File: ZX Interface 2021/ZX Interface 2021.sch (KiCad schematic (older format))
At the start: 53 parts, among them J1 PORT 1, J2 PORT 2, J4 Extended Cartridge Port, J5 JOYSTICK_EN, M1 Mounting, M2 Mounting, M3 Mounting, M4 Mounting, M5 Mounting, M6 Mounting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

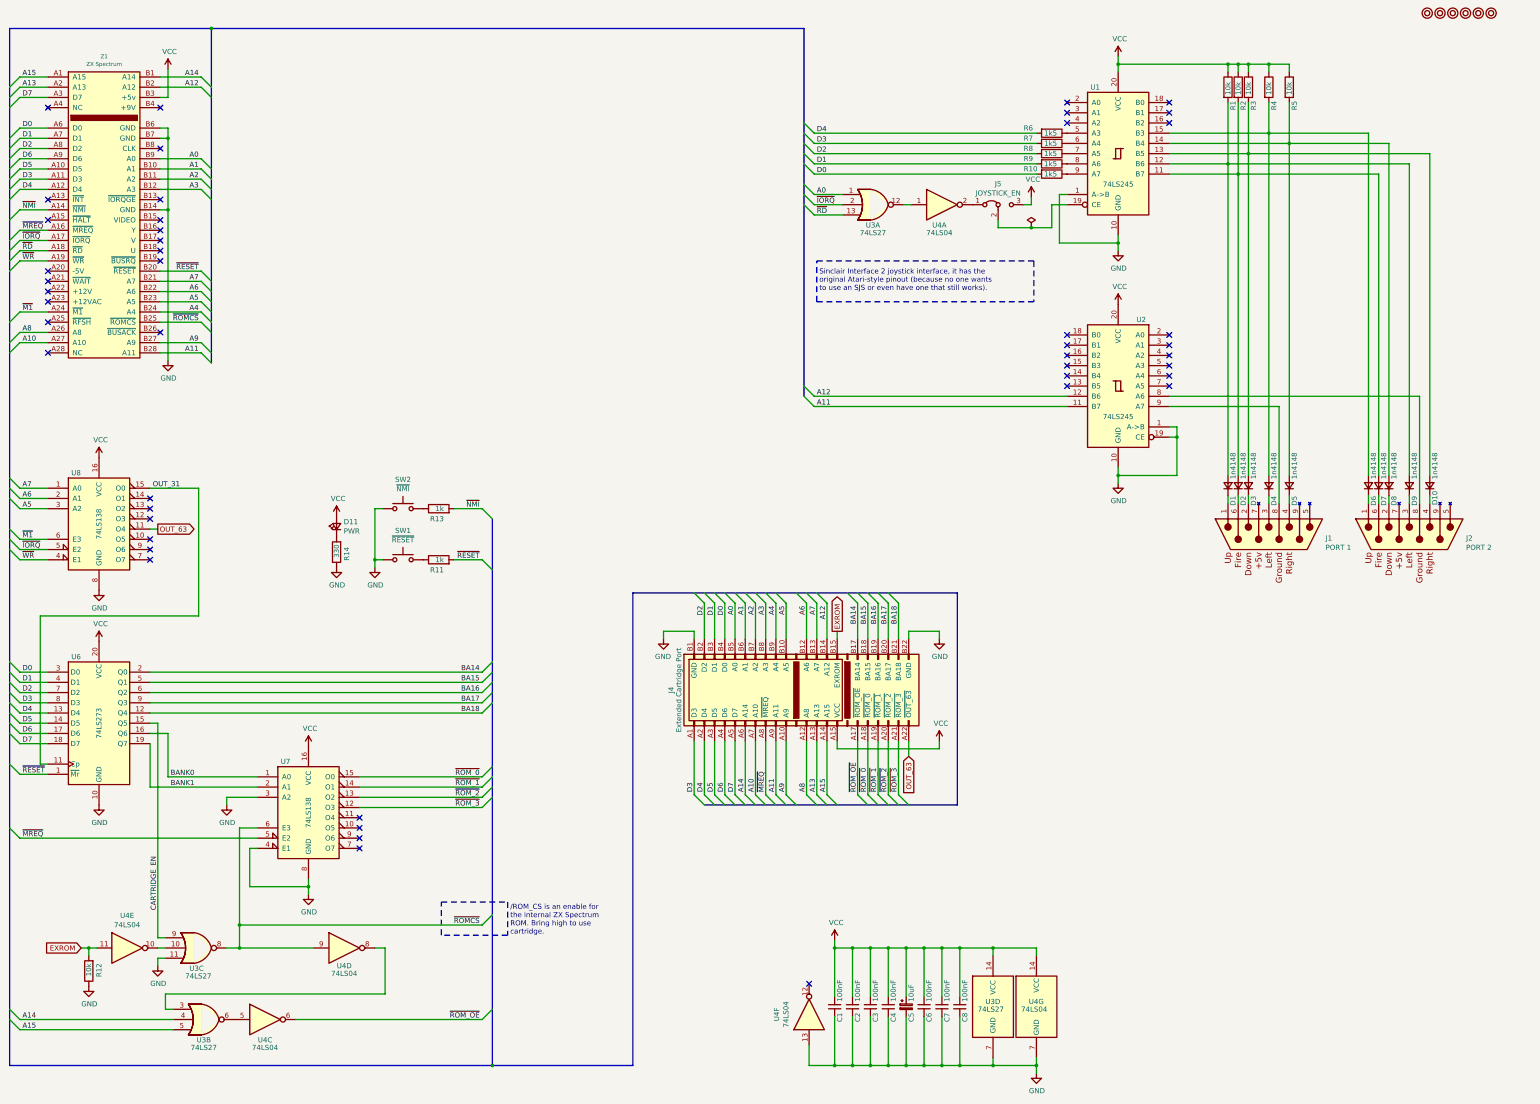
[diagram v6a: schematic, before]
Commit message: Made 74ls245 open collector instead of using resistors
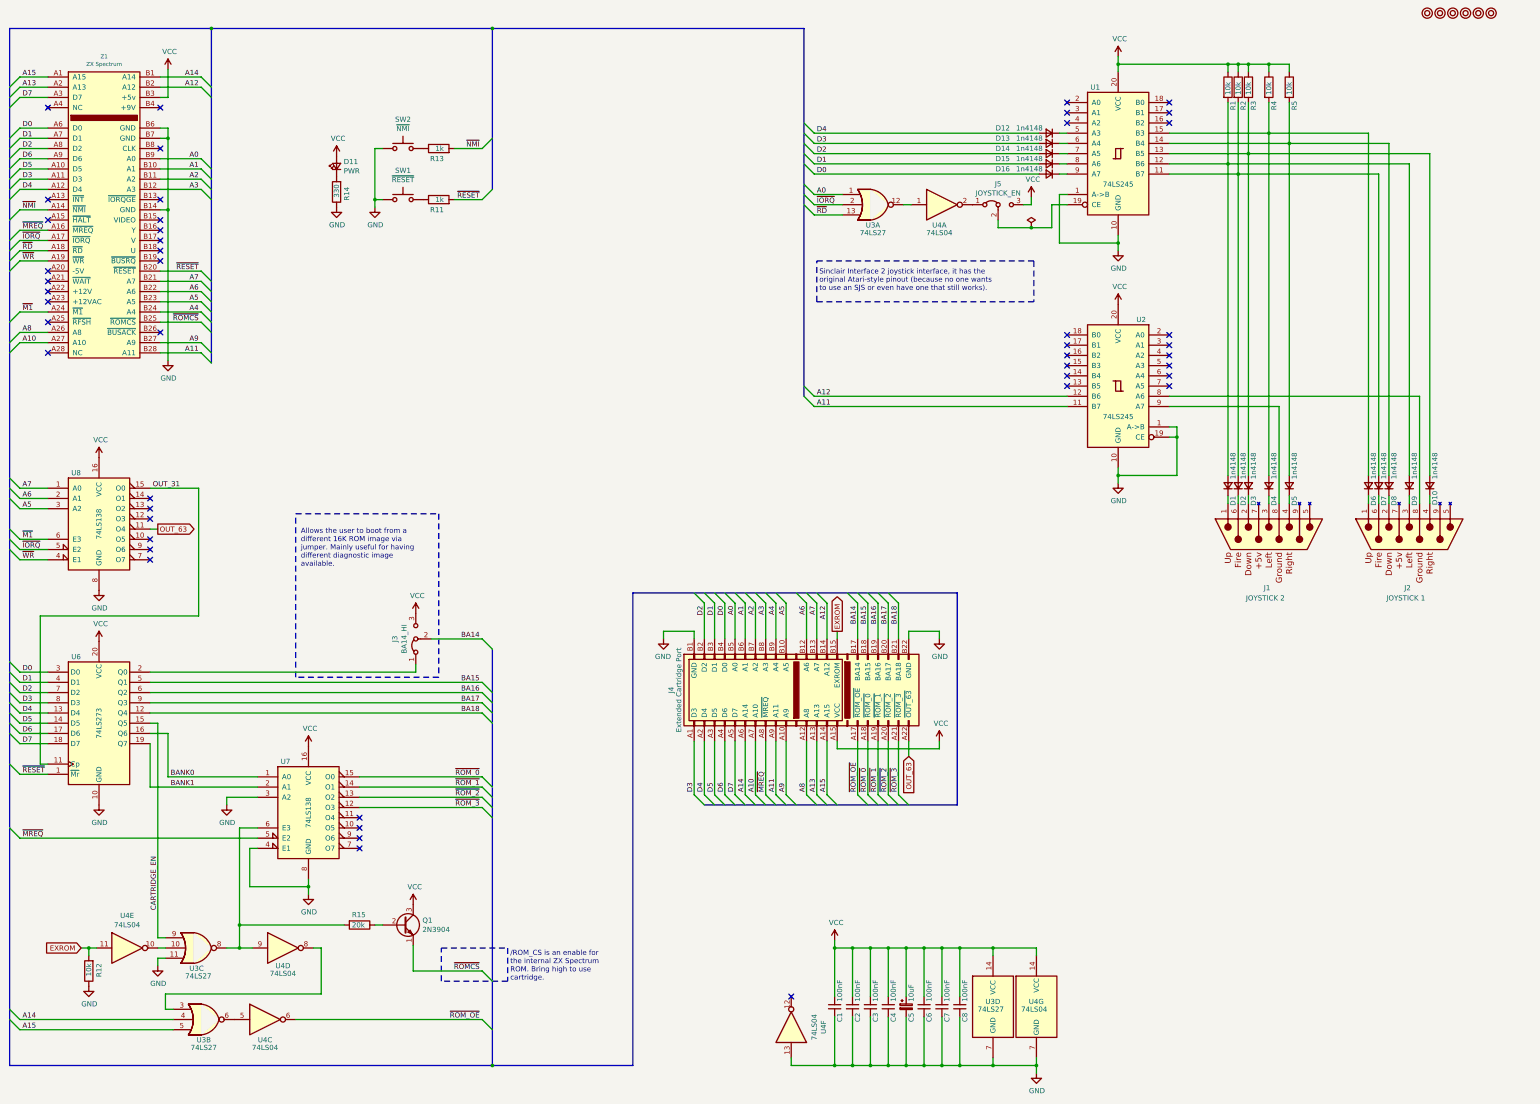
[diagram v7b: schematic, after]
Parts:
- removed R10, R6, R7, R8, R9: 1k5, Resistor_THT:R_Axial_DIN0207_L6.3mm_D2.5mm_P10.16mm_Horizontal, symbol Device:R
- added D12, D13, D14, D15, D16: 1n4148, 1n4148:D_DO-35_SOD27_P7.62mm_Horizontal, symbol Device:D_Small
- added J3: BA14_HI, Connector_PinHeader_2.54mm:PinHeader_1x03_P2.54mm_Horizontal, symbol solder_select:Jumper_3_Bridged12
- added Q1: 2N3904, Package_TO_SOT_THT:TO-92_Inline_Wide, symbol Transistor_BJT:2N3904
- added R15: 20k, Resistor_THT:R_Axial_DIN0207_L6.3mm_D2.5mm_P10.16mm_Horizontal, symbol Device:R
- J1: value PORT 1 -> JOYSTICK 2
- J2: value PORT 2 -> JOYSTICK 1
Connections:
- net BA14: now also J3.2 (C); no longer U6.2 (Q0)
- net D0: now also D16.2 (A)
- net D1: now also D15.2 (A)
- net D2: now also D14.2 (A)
- net D3: now also D13.2 (A)
- net D4: now also D12.2 (A)
- net VCC: now also J3.3 (B), Q1.3 (C)
- net ~ROMCS: now also Q1.1 (E); no longer U3.8, U4.9, U7.6 (E3)
- net at U1.5 (A3): now also D12.1 (K)
- net at U1.6 (A4): now also D13.1 (K)
- net at U1.7 (A5): now also D14.1 (K)
- net at U1.8 (A6): now also D15.1 (K)
- net at U1.9 (A7): now also D16.1 (K)
- new net: R15.2, U3.8, U4.9, U7.6 (E3)
- new net: Q1.2 (B), R15.1
- new net: J3.1 (A), U6.2 (Q0)
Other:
- note added: "Allows the user to boot from a\ndifferent 16K ROM image via\njumper. Mainly useful for having\ndifferent diagnostic image\navailable."
- moved on the sheet: D11, R11, R13, R14, SW1, SW2, U4D, U4F

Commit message: Cleanup
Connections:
- net at D7.2 (A), R2.2, U1.11 (B7): now also D4.2 (A); no longer D2.2 (A)
- net at D1.2 (A), R1.2: now also D10.2 (A), U1.14 (B4); no longer D9.2 (A), U1.12 (B6)
- net at D3.2 (A), R3.2, U1.13 (B5): now also D8.2 (A); no longer D10.2 (A)
- net at D5.2 (A), R5.2: now also D6.2 (A), U1.12 (B6); no longer D8.2 (A), U1.14 (B4)
- net at R4.2, U1.15 (B3): now also D2.2 (A), D9.2 (A); no longer D4.2 (A), D6.2 (A)
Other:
- note added: "0"
- note added: "1"
- note added: "2"
- note added: "3"
- note added: "4"
- note added: "5"
- note added: "6"
- note added: "7"
- note added: "8"
- note added: "9"
- note added: "b0"
- note added: "b1"
- note added: "b2"
- note added: "b3"
- note added: "b4"
- moved on the sheet: R2, R4
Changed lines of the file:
@@
 U 1 1 603A5F65
 P 13800 5650
-F 0 "J1" V 14325 5600 50  0000 L CNN
-F 1 "JOYSTICK 2" V 14425 5425 50  0000 L CNN
+F 0 "J1" V 14425 5600 50  0000 L CNN
+F 1 "JOYSTICK 2" V 14500 5425 50  0000 L CNN
 F 2 "RND_DSUB:DSUB-9_Male_Vertical_Pitch2.77x2.84mm" H 13800 5650 50  0001 C CNN
 F 3 "" H 13800 5650 50  0001 C CNN
@@
 U 1 1 603A8E5C
 P 15175 5650
-F 0 "J2" V 15700 5600 50  0000 L CNN
-F 1 "JOYSTICK 1" V 15800 5425 50  0000 L CNN
+F 0 "J2" V 15800 5600 50  0000 L CNN
+F 1 "JOYSTICK 1" V 15875 5425 50  0000 L CNN
 F 2 "RND_DSUB:DSUB-9_Male_Vertical_Pitch2.77x2.84mm" H 15175 5650 50  0001 C CNN
 F 3 "" H 15175 5650 50  0001 C CNN
@@
 L Device:R R2
 U 1 1 60412DFF
-P 13500 1275
-F 0 "R2" V 13550 1050 50  0000 L CNN
-F 1 "10k" V 13500 1200 50  0000 L CNN
-F 2 "Resistor_THT:R_Axial_DIN0207_L6.3mm_D2.5mm_P10.16mm_Horizontal" V 13430 1275 50  0001 C CNN
-F 3 "~" H 13500 1275 50  0001 C CNN
-	1    13500 1275
+P 13800 1275
+F 0 "R2" V 13850 1050 50  0000 L CNN
+F 1 "10k" V 13800 1200 50  0000 L CNN
+F 2 "Resistor_THT:R_Axial_DIN0207_L6.3mm_D2.5mm_P10.16mm_Horizontal" V 13730 1275 50  0001 C CNN
+F 3 "~" H 13800 1275 50  0001 C CNN
+	1    13800 1275
 	1    0    0    -1
 $EndComp
@@
 L Device:R R4
 U 1 1 60420784
-P 13800 1275
-F 0 "R4" V 13850 1050 50  0000 L CNN
-F 1 "10k" V 13800 1200 50  0000 L CNN
-F 2 "Resistor_THT:R_Axial_DIN0207_L6.3mm_D2.5mm_P10.16mm_Horizontal" V 13730 1275 50  0001 C CNN
-F 3 "~" H 13800 1275 50  0001 C CNN
-	1    13800 1275
+P 13500 1275
+F 0 "R4" V 13550 1050 50  0000 L CNN
+F 1 "10k" V 13500 1200 50  0000 L CNN
+F 2 "Resistor_THT:R_Axial_DIN0207_L6.3mm_D2.5mm_P10.16mm_Horizontal" V 13430 1275 50  0001 C CNN
+F 3 "~" H 13500 1275 50  0001 C CNN
+	1    13500 1275
 	1    0    0    -1
 $EndComp
@@
 	14000 5275 14000 5350
 Wire Wire Line
-	13800 5075 13800 1725
-Wire Wire Line
 	13600 5275 13600 5350
 Wire Wire Line
 	13500 5275 13500 5350
-Wire Wire Line
-	13400 5075 13400 2025
 Connection ~ 12325 1050
 Wire Wire Line
 	12325 1050 12325 975
-Wire Wire Line
-	14000 1425 14000 1825
-Wire Wire Line
-	13800 1425 13800 1725
-Wire Wire Line
-	13600 1425 13600 1925
-Wire Wire Line
-	13500 1425 13500 2125
-Wire Wire Line
-	13400 1425 13400 2025
 Wire Wire Line
 	12325 1125 12325 1050
@@
 Wire Wire Line
 	14000 1125 14000 1050
-Connection ~ 13800 1725
-Wire Wire Line
-	14775 1725 14775 5075
-Wire Wire Line
-	13800 1725 14775 1725
-Wire Wire Line
-	13800 1725 12825 1725
 Wire Wire Line
 	13800 5350 13800 5275
-Connection ~ 14000 1825
-Wire Wire Line
-	14975 1825 14975 5075
-Wire Wire Line
-	14000 1825 14975 1825
-Wire Wire Line
-	14000 1825 14000 5075
-Wire Wire Line
-	12825 1825 14000 1825
-Connection ~ 13600 1925
-Wire Wire Line
-	15375 1925 15375 5075
-Wire Wire Line
-	13600 1925 15375 1925
-Wire Wire Line
-	13600 1925 13600 5075
-Wire Wire Line
-	12825 1925 13600 1925
-Connection ~ 13400 2025
-Wire Wire Line
-	15175 2025 15175 5075
-Wire Wire Line
-	13400 2025 15175 2025
-Wire Wire Line
-	13400 2025 12825 2025
 Wire Wire Line
 	13400 5350 13400 5275
@@
 Wire Wire Line
 	14875 2125 14875 5075
-Wire Wire Line
-	13500 2125 14875 2125
-Connection ~ 13500 2125
-Wire Wire Line
-	13500 2125 13500 5075
-Wire Wire Line
-	12825 2125 13500 2125
 Connection ~ 12325 5075
 Wire Wire Line
@@
 Wire Wire Line
 	2850 7000 5450 7000
+$Comp
+L power:VCC #PWR0122
+U 1 1 612E5563
+P 5450 6425
+F 0 "#PWR0122" H 5450 6275 50  0001 C CNN
+F 1 "VCC" H 5465 6598 50  0000 C CNN
+F 2 "" H 5450 6425 50  0001 C CNN
+F 3 "" H 5450 6425 50  0001 C CNN
+	1    5450 6425
+	1    0    0    -1
+$EndComp
+Text Notes 13475 6200 0    50   ~ 0
+5
+Text Notes 13575 6200 0    50   ~ 0
+3
+Text Notes 13775 6200 0    50   ~ 0
+1
+Text Notes 13975 6200 0    50   ~ 0
+2
+Text Notes 14750 6200 0    50   ~ 0
+9
+Text Notes 14850 6200 0    50   ~ 0
+0
+Text Notes 14950 6200 0    50   ~ 0
+8
+Text Notes 15150 6200 0    50   ~ 0
+6
+Text Notes 15350 6200 0    50   ~ 0
+7
+Text Notes 13375 6200 0    50   ~ 0
+4
+Text Notes 13375 6250 0    31   ~ 0
+b3
+Text Notes 13475 6250 0    31   ~ 0
+b4
+Text Notes 13575 6250 0    31   ~ 0
+b2
+Text Notes 13775 6250 0    31   ~ 0
+b0
+Text Notes 13975 6250 0    31   ~ 0
+b1
+Text Notes 14750 6250 0    31   ~ 0
+b1
+Text Notes 14850 6250 0    31   ~ 0
+b0
+Text Notes 14950 6250 0    31   ~ 0
+b2
+Text Notes 15150 6250 0    31   ~ 0
+b4
+Text Notes 15350 6250 0    31   ~ 0
+b3
+Wire Wire Line
+	13800 5075 13800 2125
+Connection ~ 13800 2125
+Wire Wire Line
+	13800 2125 14875 2125
+Wire Wire Line
+	13800 1425 13800 2125
+Wire Wire Line
+	12825 2025 14000 2025
+Wire Wire Line
+	12825 2125 13800 2125
+Wire Wire Line
+	12825 1925 13600 1925
+Wire Wire Line
+	14775 5075 14775 2025
+Wire Wire Line
+	14000 5075 14000 2025
+Connection ~ 14000 2025
+Wire Wire Line
+	14000 2025 14775 2025
+Wire Wire Line
+	14000 2025 14000 1425
+Wire Wire Line
+	14975 5075 14975 1925
+Wire Wire Line
+	13600 5075 13600 1925
+Connection ~ 13600 1925
+Wire Wire Line
+	13600 1925 14975 1925
+Wire Wire Line
+	13600 1925 13600 1425
+Wire Wire Line
+	15375 5075 15375 1825
+Wire Wire Line
+	12825 1825 13400 1825
+Wire Wire Line
+	13400 5075 13400 1825
+Connection ~ 13400 1825
+Wire Wire Line
+	13400 1825 15375 1825
+Wire Wire Line
+	13400 1825 13400 1425
+Wire Wire Line
+	15175 5075 15175 1725
+Wire Wire Line
+	12825 1725 13500 1725
+Wire Wire Line
+	13500 5075 13500 1725
+Connection ~ 13500 1725
+Wire Wire Line
+	13500 1725 15175 1725
+Wire Wire Line
+	13500 1725 13500 1425
 Wire Bus Line
 	6200 700  6200 2275
@@
 Wire Bus Line
 	1475 700  1475 10850
-$Comp
-L power:VCC #PWR0122
-U 1 1 612E5563
-P 5450 6425
-F 0 "#PWR0122" H 5450 6275 50  0001 C CNN
-F 1 "VCC" H 5465 6598 50  0000 C CNN
-F 2 "" H 5450 6425 50  0001 C CNN
-F 3 "" H 5450 6425 50  0001 C CNN
-	1    5450 6425
-	1    0    0    -1
-$EndComp
 $EndSCHEMATC
